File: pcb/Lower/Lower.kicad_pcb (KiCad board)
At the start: 2 copper layers, 52 x 42 mm, 35 parts, among them J1 AudioJack3, J2 AudioJack3, J3 Barrel_Jack, J4 Conn_01x04, Q1 AO3401A, SW1 SW_Push_3PDT, U1 TL072

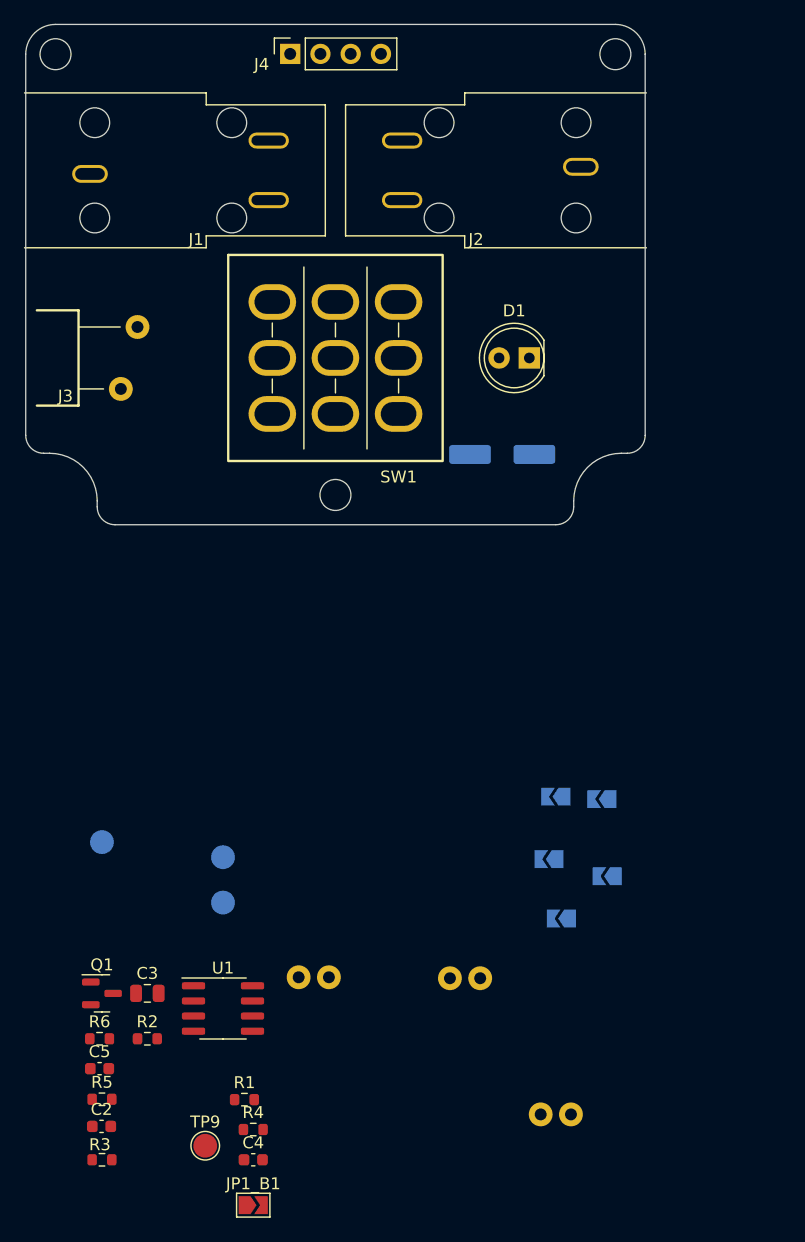
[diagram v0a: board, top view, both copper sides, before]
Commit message: [Lower] Make PCB smaller
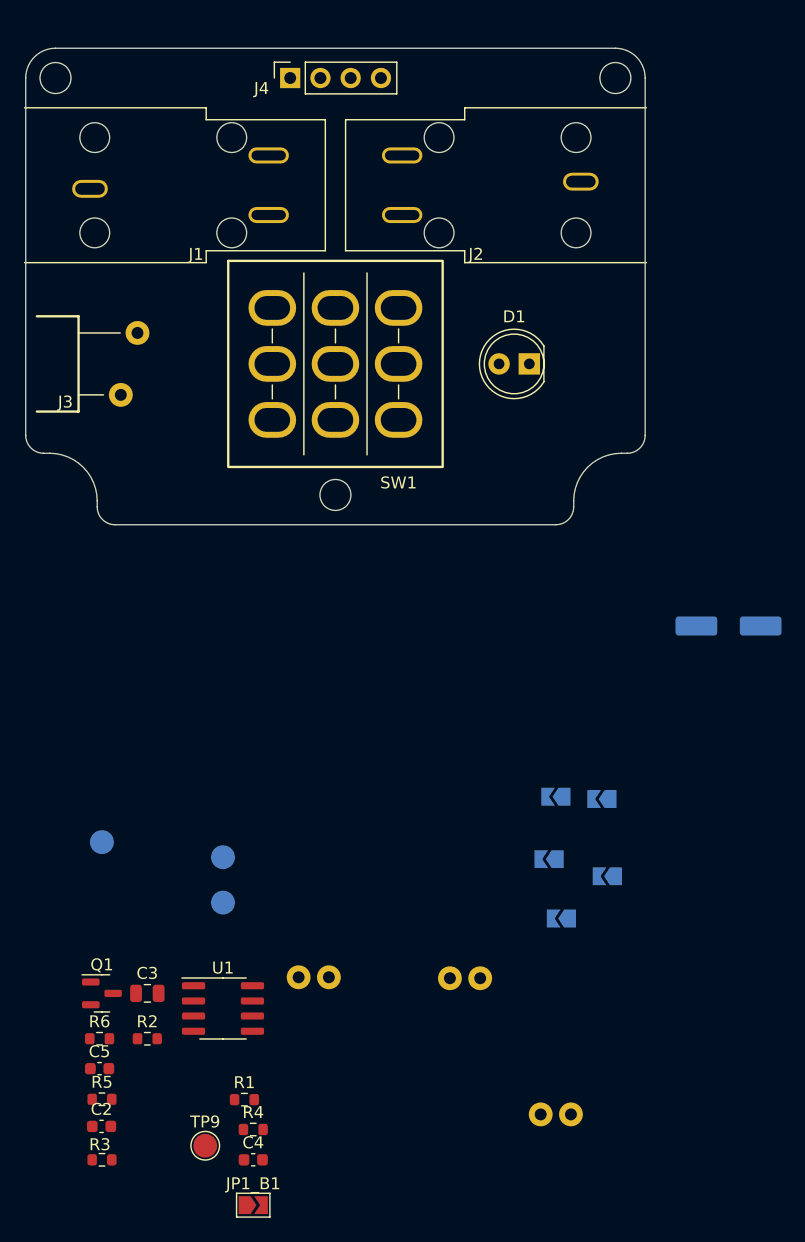
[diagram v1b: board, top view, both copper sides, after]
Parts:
- moved C1 23.8 mm to (182.5, 130.5)
- moved J4 2.03 mm to (145.7, 84.5)
- moved MK2 2.00 mm to (126.0, 84.5)
- moved MK2 2.00 mm to (173.0, 84.5)
- moved J1 1.25 mm to (128.9, 93.5)
- moved J2 1.25 mm to (170.1, 93.5)
- moved D1 0.50 mm to (165.8, 108.5)
- moved J3 0.50 mm to (127.9, 108.5)
- moved SW1 0.50 mm to (149.5, 108.5)
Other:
- board size 52 x 42 mm -> 52 x 40 mm
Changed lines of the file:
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@@
     (pad_to_mask_clearance 0.05)
     (solder_mask_min_width 0.254)
-    (aux_axis_origin 149.5 108)
-    (grid_origin 149.5 108)
+    (aux_axis_origin 149.5 108.5)
+    (grid_origin 149.5 108.5)
     (pcbplotparams
       (layerselection 0x00010fc_ffffffff)
@@
   )
   (footprint "Connector_PinSocket_2.54mm:PinSocket_1x04_P2.54mm_Vertical" (layer "F.Cu")
-    (at 145.7 82.475 90)
+    (at 145.7 84.5 90)
     (descr "Through hole straight socket strip, 1x04, 2.54mm pitch, single row (from Kicad 4.0.7), script generated")
     (tags "Through hole socket strip THT 1x04 2.54mm single row")
@@
   )
   (footprint "MeineBib:EigenesMountingHole_2.6mm_M2.5_Small" (layer "F.Cu")
-    (at 126 82.5)
+    (at 126 84.5)
     (descr "Mounting Hole 2.7mm, no annular, M2.5")
     (tags "mounting hole 2.7mm no annular m2.5")
@@
   )
   (footprint "MeineBib:EigenesMountingHole_2.6mm_M2.5_Small" (layer "F.Cu")
-    (at 173 82.5)
+    (at 173 84.5)
     (descr "Mounting Hole 2.7mm, no annular, M2.5")
     (tags "mounting hole 2.7mm no annular m2.5")
@@
   )
   (footprint "MeineBib:Footswitch_3PDT" (layer "B.Cu")
-    (at 149.5 108 180)
+    (at 149.5 108.5 180)
     (property "Sheetfile" "Lower.kicad_sch")
     (property "Sheetname" "")
@@
   )
   (footprint "LED_THT:LED_D5.0mm" (layer "B.Cu")
-    (at 165.775 108 180)
+    (at 165.775 108.5 180)
     (descr "LED, diameter 5.0mm, 2 pins, http://cdn-reichelt.de/documents/datenblatt/A500/LL-504BC2E-009.pdf")
     (tags "LED diameter 5.0mm 2 pins")
@@
   )
   (footprint "MeineBib:DC_Barrel_Jack_Thinline_Wired_Standing" (layer "B.Cu")
-    (at 127.933 108 180)
+    (at 127.933 108.5 180)
     (property "Sheetfile" "Lower.kicad_sch")
     (property "Sheetname" "")
@@
   )
   (footprint "Capacitor_SMD:CP_Elec_6.3x5.8" (layer "B.Cu")
-    (at 163.5 116.1 180)
+    (at 182.5 130.5 180)
     (descr "SMD capacitor, aluminum electrolytic, Nichicon, 6.3x5.8mm")
     (tags "capacitor electrolytic")
@@
   )
   (footprint "MeineBib:Audio_Jack_PJ-602B" (layer "B.Cu")
-    (at 128.895 92.25 180)
+    (at 128.895 93.5 180)
     (property "Sheetfile" "Lower.kicad_sch")
     (property "Sheetname" "")
@@
   )
   (footprint "MeineBib:Audio_Jack_PJ-602B" (layer "B.Cu")
-    (at 170.1 92.25)
+    (at 170.1 93.5)
     (property "Sheetfile" "Lower.kicad_sch")
     (property "Sheetname" "")
@@
       ))
   )
-  (gr_line (start 138.65 85.75) (end 138.65 86.75) (layer "F.SilkS") (width 0.12))
-  (gr_line (start 160.35 85.75) (end 160.35 86.75) (layer "F.SilkS") (width 0.12))
-  (gr_line (start 123.4 85.75) (end 138.65 85.75) (layer "F.SilkS") (width 0.12))
-  (gr_line (start 160.35 97.75) (end 160.35 98.75) (layer "F.SilkS") (width 0.12))
-  (gr_line (start 160.35 98.75) (end 175.6 98.75) (layer "F.SilkS") (width 0.12))
-  (gr_line (start 160.35 86.75) (end 150.35 86.75) (layer "F.SilkS") (width 0.12))
-  (gr_line (start 130.033 110.6) (end 127.933 110.6) (layer "F.SilkS") (width 0.12))
-  (gr_line (start 138.65 86.75) (end 148.65 86.75) (layer "F.SilkS") (width 0.12))
-  (gr_line (start 127.933 104) (end 127.933 112) (layer "F.SilkS") (width 0.2))
-  (gr_line (start 150.35 97.75) (end 160.35 97.75) (layer "F.SilkS") (width 0.12))
-  (gr_arc (start 166.999999 109.5) (mid 161.584525 108) (end 166.999999 106.5) (layer "F.SilkS") (width 0.12))
-  (gr_line (start 150.35 86.75) (end 150.35 97.75) (layer "F.SilkS") (width 0.12))
-  (gr_line (start 166.999999 109.5) (end 166.999999 106.5) (layer "F.SilkS") (width 0.12))
-  (gr_line (start 127.933 112) (end 124.433 112) (layer "F.SilkS") (width 0.2))
-  (gr_line (start 138.65 97.75) (end 138.65 98.75) (layer "F.SilkS") (width 0.12))
-  (gr_line (start 148.65 86.75) (end 148.65 97.75) (layer "F.SilkS") (width 0.12))
-  (gr_line (start 148.65 97.75) (end 138.65 97.75) (layer "F.SilkS") (width 0.12))
-  (gr_line (start 175.6 85.75) (end 160.35 85.75) (layer "F.SilkS") (width 0.12))
-  (gr_line (start 124.433 104) (end 127.933 104) (layer "F.SilkS") (width 0.2))
-  (gr_line (start 138.65 98.75) (end 123.4 98.75) (layer "F.SilkS") (width 0.12))
-  (gr_line (start 131.433 105.4) (end 127.933 105.4) (layer "F.SilkS") (width 0.12))
-  (gr_circle (center 164.5 108) (end 162 107.9) (layer "F.SilkS") (width 0.12) (fill none))
-  (gr_line (start 149.5 78.75) (end 149.5 126.75) (layer "Eco1.User") (width 0.15))
+  (gr_line (start 138.65 87) (end 138.65 88) (layer "F.SilkS") (width 0.12))
+  (gr_line (start 160.35 87) (end 160.35 88) (layer "F.SilkS") (width 0.12))
+  (gr_line (start 123.4 87) (end 138.65 87) (layer "F.SilkS") (width 0.12))
+  (gr_line (start 160.35 99) (end 160.35 100) (layer "F.SilkS") (width 0.12))
+  (gr_line (start 160.35 100) (end 175.6 100) (layer "F.SilkS") (width 0.12))
+  (gr_line (start 160.35 88) (end 150.35 88) (layer "F.SilkS") (width 0.12))
+  (gr_line (start 130.033 111.1) (end 127.933 111.1) (layer "F.SilkS") (width 0.12))
+  (gr_line (start 138.65 88) (end 148.65 88) (layer "F.SilkS") (width 0.12))
+  (gr_line (start 127.933 104.5) (end 127.933 112.5) (layer "F.SilkS") (width 0.2))
+  (gr_line (start 150.35 99) (end 160.35 99) (layer "F.SilkS") (width 0.12))
+  (gr_arc (start 166.999999 110) (mid 161.584525 108.5) (end 166.999999 107) (layer "F.SilkS") (width 0.12))
+  (gr_line (start 150.35 88) (end 150.35 99) (layer "F.SilkS") (width 0.12))
+  (gr_line (start 166.999999 110) (end 166.999999 107) (layer "F.SilkS") (width 0.12))
+  (gr_line (start 127.933 112.5) (end 124.433 112.5) (layer "F.SilkS") (width 0.2))
+  (gr_line (start 138.65 99) (end 138.65 100) (layer "F.SilkS") (width 0.12))
+  (gr_line (start 148.65 88) (end 148.65 99) (layer "F.SilkS") (width 0.12))
+  (gr_line (start 148.65 99) (end 138.65 99) (layer "F.SilkS") (width 0.12))
+  (gr_line (start 175.6 87) (end 160.35 87) (layer "F.SilkS") (width 0.12))
+  (gr_line (start 124.433 104.5) (end 127.933 104.5) (layer "F.SilkS") (width 0.2))
+  (gr_line (start 138.65 100) (end 123.4 100) (layer "F.SilkS") (width 0.12))
+  (gr_line (start 131.433 105.9) (end 127.933 105.9) (layer "F.SilkS") (width 0.12))
+  (gr_circle (center 164.5 108.5) (end 162 108.4) (layer "F.SilkS") (width 0.12) (fill none))
+  (gr_line (start 149.5 80.5) (end 149.5 126.75) (layer "Eco1.User") (width 0.15))
+  (gr_line (start 177.5 93.5) (end 121.5 93.5) (layer "Eco1.User") (width 0.15))
+  (gr_line (start 177.5 108.5) (end 121.5 108.5) (layer "Eco1.User") (width 0.15))
   (gr_line (start 129.5 120) (end 129.5 120.5) (layer "Edge.Cuts") (width 0.1))
   (gr_arc (start 125.5 116) (mid 128.328427 117.171573) (end 129.5 120) (layer "Edge.Cuts") (width 0.1))
   (gr_line (start 174 116) (end 173.5 116) (layer "Edge.Cuts") (width 0.1))
-  (gr_line (start 175.5 82.5) (end 175.5 114.5) (layer "Edge.Cuts") (width 0.1))
+  (gr_line (start 175.5 84.5) (end 175.5 114.5) (layer "Edge.Cuts") (width 0.1))
   (gr_arc (start 169.5 120) (mid 170.671573 117.171573) (end 173.5 116) (layer "Edge.Cuts") (width 0.1))
-  (gr_line (start 123.5 82.5) (end 123.5 114.5) (layer "Edge.Cuts") (width 0.1))
+  (gr_line (start 123.5 84.5) (end 123.5 114.5) (layer "Edge.Cuts") (width 0.1))
   (gr_arc (start 131 122) (mid 129.93934 121.56066) (end 129.5 120.5) (layer "Edge.Cuts") (width 0.1))
-  (gr_line (start 126 80) (end 173 80) (layer "Edge.Cuts") (width 0.1))
-  (gr_arc (start 123.5 82.5) (mid 124.232233 80.732233) (end 126 80) (layer "Edge.Cuts") (width 0.1))
+  (gr_line (start 126 82) (end 173 82) (layer "Edge.Cuts") (width 0.1))
+  (gr_arc (start 123.5 84.5) (mid 124.232233 82.732233) (end 126 82) (layer "Edge.Cuts") (width 0.1))
   (gr_arc (start 125 116) (mid 123.93934 115.56066) (end 123.5 114.5) (layer "Edge.Cuts") (width 0.1))
   (gr_arc (start 169.5 120.5) (mid 169.06066 121.56066) (end 168 122) (layer "Edge.Cuts") (width 0.1))
-  (gr_arc (start 173 80) (mid 174.767767 80.732233) (end 175.5 82.5) (layer "Edge.Cuts") (width 0.1))
+  (gr_arc (start 173 82) (mid 174.767767 82.732233) (end 175.5 84.5) (layer "Edge.Cuts") (width 0.1))
   (gr_line (start 169.5 120) (end 169.5 120.5) (layer "Edge.Cuts") (width 0.1))
   (gr_line (start 131 122) (end 168 122) (layer "Edge.Cuts") (width 0.1))
   (gr_line (start 125 116) (end 125.5 116) (layer "Edge.Cuts") (width 0.1))
   (gr_arc (start 175.5 114.5) (mid 175.06066 115.56066) (end 174 116) (layer "Edge.Cuts") (width 0.1))
+  (dimension (type aligned) (layer "Eco1.User")
+    (pts (xy 149.5 108.5) (xy 149.5 93.5))
+    (height -40)
+    (gr_text "15.0000 mm" (at 108.35 101 90) (layer "Eco1.User")
+      (effects (font (size 1 1) (thickness 0.15)))
+    )
+    (format (units 3) (units_format 1) (precision 4))
+    (style (thickness 0.15) (arrow_length 1.27) (text_position_mode 0) (extension_height 0.58642) (extension_offset 0.5) keep_text_aligned)
+  )
+  (dimension (type aligned) (layer "Eco1.User")
+    (pts (xy 139.5 108.5) (xy 139.5 122))
+    (height 30)
+    (gr_text "13.5000 mm" (at 108.35 115.25 90) (layer "Eco1.User")
+      (effects (font (size 1 1) (thickness 0.15)))
+    )
+    (format (units 3) (units_format 1) (precision 4))
+    (style (thickness 0.15) (arrow_length 1.27) (text_position_mode 0) (extension_height 0.58642) (extension_offset 0.5) keep_text_aligned)
+  )
+  (dimension (type aligned) (layer "Eco1.User")
+    (pts (xy 149.5 108.5) (xy 164.5 108.5))
+    (height 25.5)
+    (gr_text "15.0000 mm" (at 157 132.85) (layer "Eco1.User")
+      (effects (font (size 1 1) (thickness 0.15)))
+    )
+    (format (units 3) (units_format 1) (precision 4))
+    (style (thickness 0.15) (arrow_length 1.27) (text_position_mode 0) (extension_height 0.58642) (extension_offset 0.5) keep_text_aligned)
+  )
   (group "" (id 13853ac3-03d5-4fa8-a1c3-000a9dab54c6)
     (members
@@
     )
   )
+  (group "" (id a73d2e16-8c97-4165-98d0-30fdad0408a8)
+    (members
+      71e07d2b-8cad-4312-b685-de664e921038
+      771f4e12-2fd6-4399-9b3b-26b9df9aa127
+      86031470-f583-4188-9340-4bfd67a8bb4d
+      fc2102e1-d912-471d-a6d1-254b75955533
+    )
+  )

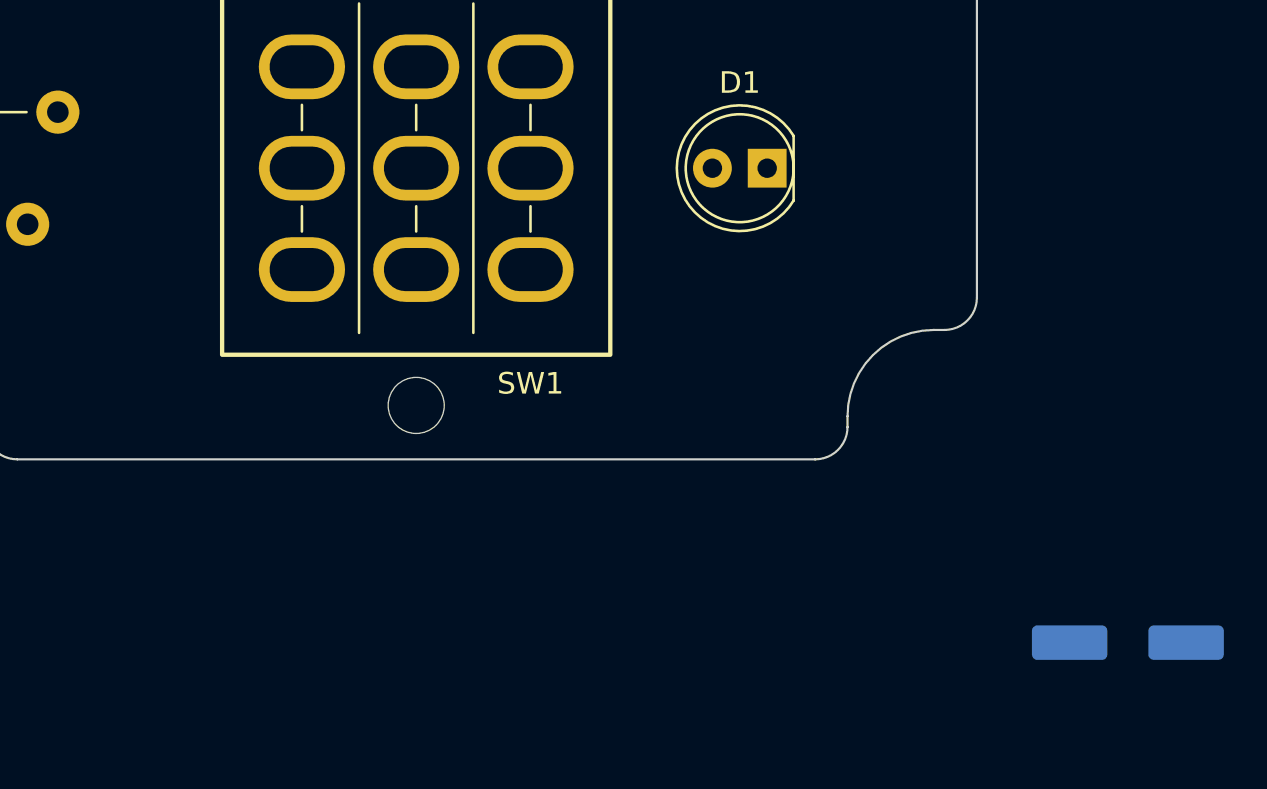
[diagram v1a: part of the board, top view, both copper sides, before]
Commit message: [Lower] Swap out C1 footprint / LCSC part for THT one
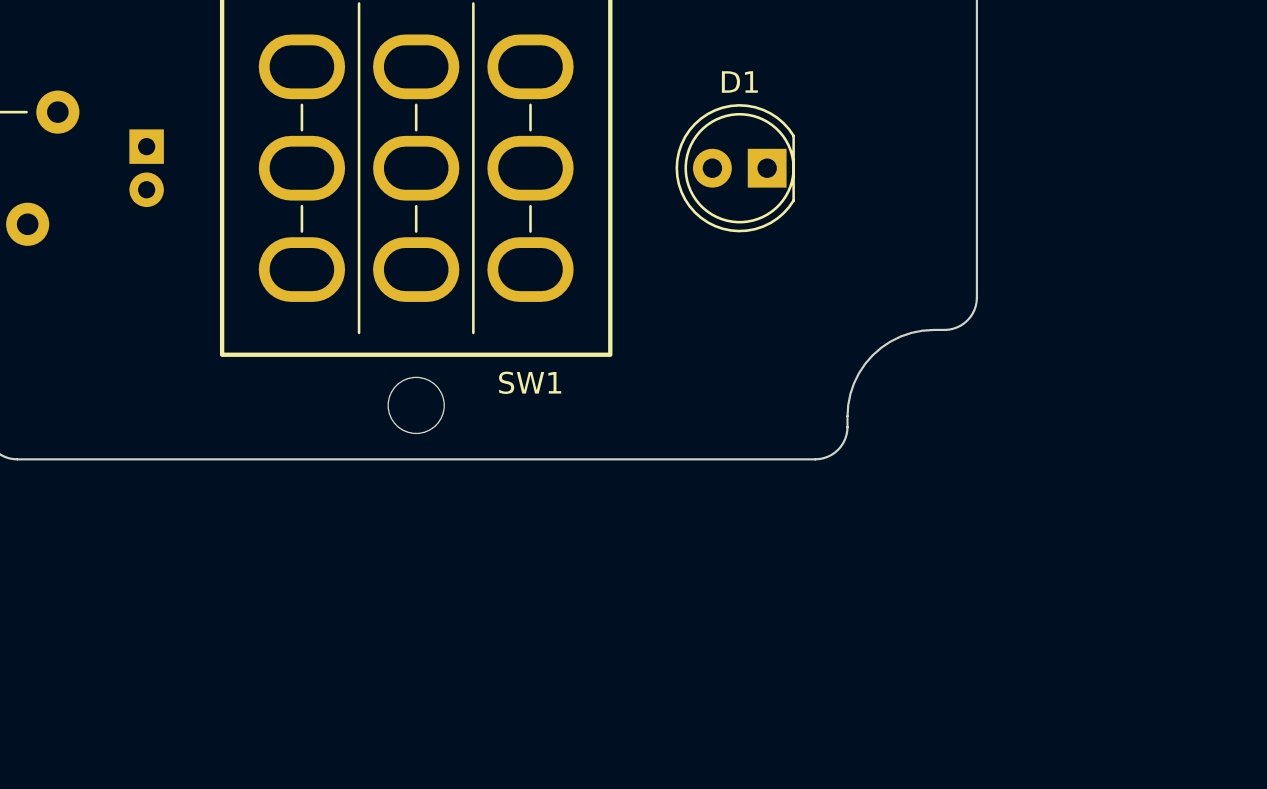
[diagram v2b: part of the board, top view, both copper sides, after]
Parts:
- C1: footprint Capacitor_SMD:CP_Elec_6.3x5.8 -> Capacitor_THT:CP_Radial_D5.0mm_P2.00mm
- moved C1 51.0 mm to (137.0, 107.5), turned to -90 degrees
